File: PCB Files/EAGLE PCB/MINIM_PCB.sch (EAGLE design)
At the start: 22 parts, among them IC1 4066D, IC2 OP-AMP

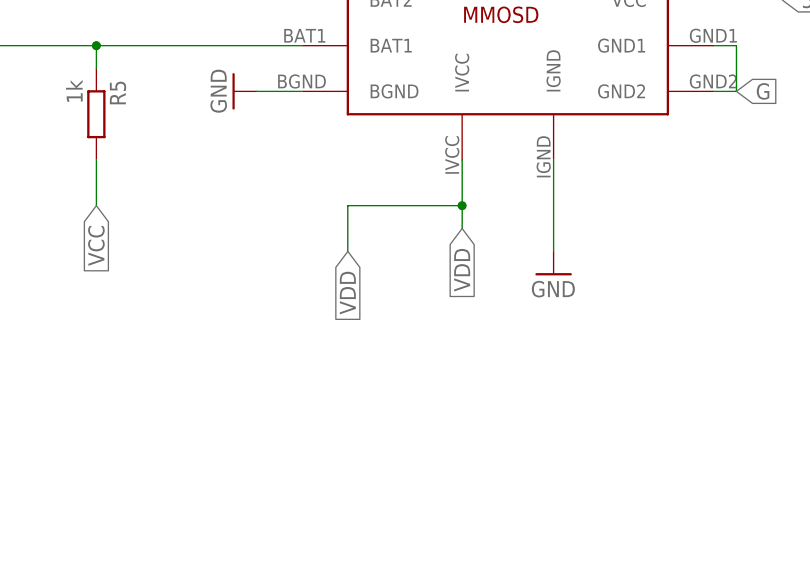
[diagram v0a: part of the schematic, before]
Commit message: new pcb1 revision 3 (5v on RJ45 and OSD PCB footprint added)
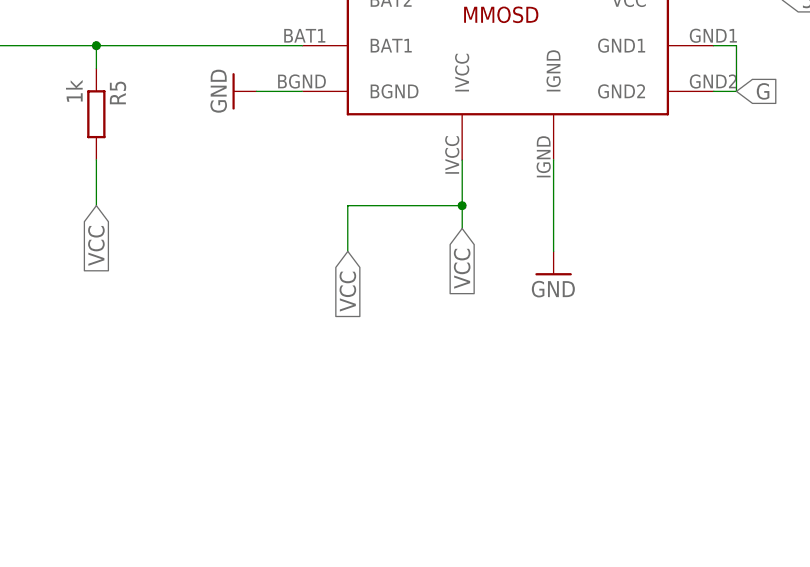
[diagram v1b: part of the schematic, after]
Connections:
- net N$5 renamed VIDIN_AMP
- removed net VDD: MINIMOSD.IVCC
- net VCC: now also MINIMOSD.IVCC
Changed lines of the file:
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@@
 <label x="210.82" y="111.76" size="1.778" layer="95" rot="R270" xref="yes"/>
+</segment>
+<segment>
+<pinref part="MINIMOSD" gate="G$1" pin="IVCC"/>
+<wire x1="251.46" y1="116.84" x2="251.46" y2="111.76" width="0.1524" layer="91"/>
+<label x="251.46" y="109.22" size="1.778" layer="95" rot="R270" xref="yes"/>
+<wire x1="251.46" y1="111.76" x2="251.46" y2="109.22" width="0.1524" layer="91"/>
+<wire x1="251.46" y1="111.76" x2="238.76" y2="111.76" width="0.1524" layer="91"/>
+<junction x="251.46" y="111.76"/>
+<wire x1="238.76" y1="111.76" x2="238.76" y2="106.68" width="0.1524" layer="91"/>
+<label x="238.76" y="106.68" size="1.778" layer="95" rot="R270" xref="yes"/>
 </segment>
 </net>
@@
 </segment>
 </net>
-<net name="N$5" class="0">
+<net name="VIDIN_AMP" class="0">
 <segment>
 <pinref part="R7" gate="G$1" pin="1"/>
@@
 </segment>
 </net>
-<net name="VDD" class="0">
-<segment>
-<pinref part="MINIMOSD" gate="G$1" pin="IVCC"/>
-<wire x1="251.46" y1="116.84" x2="251.46" y2="111.76" width="0.1524" layer="91"/>
-<label x="251.46" y="109.22" size="1.778" layer="95" rot="R270" xref="yes"/>
-<wire x1="251.46" y1="111.76" x2="251.46" y2="109.22" width="0.1524" layer="91"/>
-<wire x1="251.46" y1="111.76" x2="238.76" y2="111.76" width="0.1524" layer="91"/>
-<junction x="251.46" y="111.76"/>
-<wire x1="238.76" y1="111.76" x2="238.76" y2="106.68" width="0.1524" layer="91"/>
-<label x="238.76" y="106.68" size="1.778" layer="95" rot="R270" xref="yes"/>
-</segment>
-</net>
